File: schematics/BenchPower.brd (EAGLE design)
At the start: 80 x 67 mm, 30 parts, among them U1 V_REG_317SINK, U2 V_REG_317SINK, X2 9090-4R

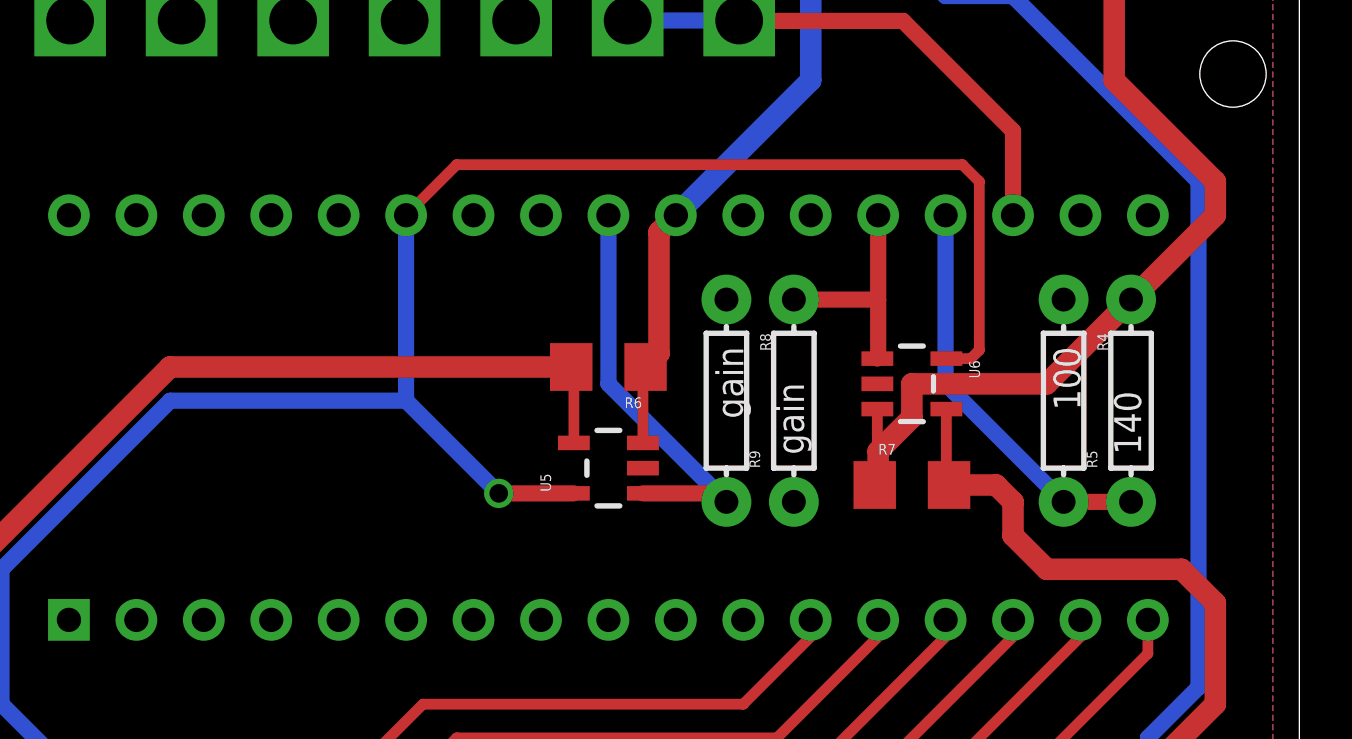
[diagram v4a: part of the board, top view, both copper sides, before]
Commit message: Rework opamp layout
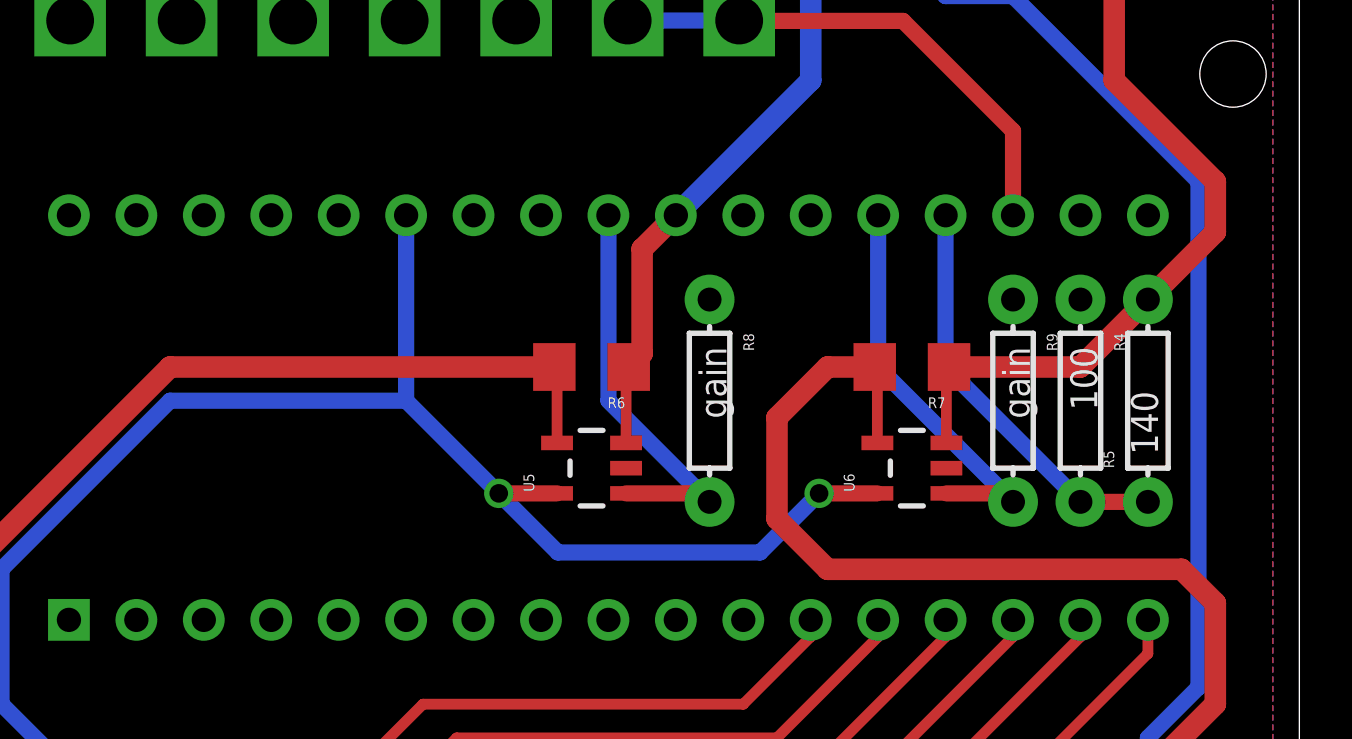
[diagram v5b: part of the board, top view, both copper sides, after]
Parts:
- moved R9 8.26 mm to (69.2, 36.2), turned to 270 degrees
- moved R7 4.45 mm to (65.4, 37.5), turned to 180 degrees
- moved U6 3.17 mm to (65.4, 33.7), turned to 90 degrees
- moved R5 0.64 mm to (74.3, 36.2)
- moved R8 0.64 mm to (57.8, 36.2)
- moved R6 0.63 mm to (53.3, 37.5)
- moved U5 0.63 mm to (53.3, 33.7)
- moved R4 0.63 mm to (71.8, 36.2)
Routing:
- net 5VARDU: track 113.1 -> 98.2 mm, vias 1 -> 2
- net AMPS12VREG: track 48.0 -> 61.5 mm
- net 12VCURRENT: track 8.59 -> 15.5 mm
- net 12VREG: track 49.3 -> 44.8 mm
- net AMPS5VREG: track 56.7 -> 56.1 mm

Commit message: Route signals
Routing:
- net 12VREG: track 44.8 -> 45.5 mm
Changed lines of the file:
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@@
 <wire x1="76.835" y1="44.45" x2="76.835" y2="42.545" width="0.8128" layer="1"/>
 <wire x1="76.835" y1="42.545" x2="74.295" y2="40.005" width="0.8128" layer="1"/>
-<wire x1="74.295" y1="40.005" x2="71.755" y2="37.465" width="0.8128" layer="1"/>
-<wire x1="71.755" y1="37.465" x2="66.805" y2="37.465" width="0.8128" layer="1"/>
+<wire x1="73.025" y1="37.465" x2="66.805" y2="37.465" width="0.8128" layer="1"/>
 <wire x1="66.7051" y1="34.605" x2="66.7051" y2="37.3651" width="0.4064" layer="1"/>
 <wire x1="66.7051" y1="37.3651" x2="66.805" y2="37.465" width="0.4064" layer="1"/>
+<wire x1="73.025" y1="37.465" x2="74.295" y2="38.735" width="0.8128" layer="1"/>
+<wire x1="74.295" y1="38.735" x2="74.295" y2="40.005" width="0.8128" layer="1"/>
 </signal>
 <signal name="ADJREG1">

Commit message: Simplify
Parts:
- removed JP2, JP3: (no value), SparkFun-Connectors:1X03
- removed RV4: (no value), desjardins:POTRK09K111
- removed U2: V_REG_317SINK, SparkFun-PowerIC:TO220-ADJ
- added R10: 140, SparkFun-Passives:AXIAL-0.3
- added S1: EG1213, adafruit:EG1213
- R3: value 240 -> 100
- moved R3 41.2 mm to (50.8, 45.7), turned to 0 degrees
- moved X2 27.4 mm to (12.7, 60.3), turned to 0 degrees
- moved U1 8.48 mm to (77.5, 61.6)
- moved U$1 8.26 mm to (48.3, 55.9)
- moved R2 4.58 mm to (73.0, 55.2), turned to 270 degrees
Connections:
- net 12VCURRENT renamed 12VREGCURRENT
- net 5VCURRENT renamed 12VHDRCURRENT
- net AMPS5VREG renamed AMPS12VHDR
- removed net 12VHDRREG: JP2.3, U1.IN
- removed net 5VHDRREG: JP3.3, U2.IN
- removed net 5VREG: JP3.1, R3.P$2, R6.1, U$2.P25, U2.OUT, U5.3
- removed net ADJREG2: R3.P$1, RV4.P$2, U2.ADJ
- removed net PUSHBUTTON: U$2.P11
- removed net VIN: U$2.P32
- new net 12VHDRSW: R10.P$2, R6.1, S1.2, U1.IN, U5.3
- new net 12VHDRTAP: R10.P$1, R3.P$2, U$2.P25
- net 12VHDR: now also S1.1, U$2.P32; no longer JP2.2
- net 12VREG: no longer JP2.1
- net 5VHDR: no longer JP3.2
- net GND: now also R3.P$1; no longer RV4.P$3
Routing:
- net 12VHDRSW: track 0.00 -> 131.1 mm
- net 5VREG: track 94.2 -> 0.00 mm
- net ADJREG2: track 67.1 -> 0.00 mm
- net 5VHDR: track 138.1 -> 107.5 mm
- net 12VHDR: track 93.3 -> 111.2 mm, vias 0 -> 1
- net 5VHDRREG: track 10.1 -> 0.00 mm
- net 12VHDRREG: track 8.36 -> 0.00 mm
- net 12VREG: track 45.5 -> 39.0 mm
- net 12VHDRTAP: track 0.00 -> 6.35 mm
- net AMPS12VHDR: track 56.1 -> 57.6 mm
- net ADJREG1: track 66.1 -> 64.6 mm
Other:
- board text added: "adj"
- board text removed: "5v"
- board text removed: "bypass"

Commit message: Final pass
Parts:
- removed S1: EG1213, adafruit:EG1213
- added S2: EG1213, desjardins:EG1213
- R1: value 100 -> 1000
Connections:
- net 12VHDR: now also S2.1; no longer S1.1
- net 12VHDRSW: now also R1.P$1, S2.2; no longer S1.2
- net 5VHDR: no longer R1.P$1
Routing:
- net 5VHDR: track 107.5 -> 65.2 mm
- net 12VHDRSW: track 131.1 -> 155.6 mm
- net 12VHDR: track 111.2 -> 108.0 mm
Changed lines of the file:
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@@
 <wire x1="80" y1="67" x2="0" y2="67" width="0" layer="20"/>
 <wire x1="0" y1="67" x2="0" y2="0" width="0" layer="20"/>
-<text x="42.545" y="12.7" size="1.27" layer="21" font="vector">cjd@chrisd.info</text>
-<text x="1.27" y="1.27" size="1.27" layer="21" font="vector">v1.0 (c) 2014</text>
+<text x="43.18" y="12.7" size="1.524" layer="21">cjd@chrisd.info</text>
+<text x="1.27" y="1.27" size="1.27" layer="21">v1.0 (c) 2014</text>
 <wire x1="13.97" y1="5.715" x2="13.97" y2="5.97" width="0.4064" layer="21"/>
 <wire x1="13.97" y1="5.97" x2="20" y2="12" width="0.4064" layer="21" curve="-90"/>
@@
 <wire x1="60" y1="0" x2="47" y2="0" width="0.4064" layer="21"/>
 <wire x1="47" y1="0" x2="41" y2="6" width="0.4064" layer="21" curve="-90"/>
-<text x="52.07" y="1.27" size="1.27" layer="21" font="vector">adj</text>
-<text x="24.765" y="1.27" size="1.27" layer="21" font="vector">12v</text>
-<text x="10.795" y="12.7" size="1.27" layer="21" font="vector">blog.chrisd.info</text>
+<text x="52.07" y="1.27" size="1.27" layer="21">adj</text>
+<text x="24.765" y="1.27" size="1.27" layer="21">12v</text>
+<text x="10.795" y="12.7" size="1.524" layer="21">blog.chrisd.info</text>
 </plain>
 <attributes>
@@
 <element name="U$2" library="ChrisD" package="ARDUINO_PRO_MICRO" value="ARDUINO_PRO_MICRO" x="78.105" y="26.67" rot="R90"/>
 <element name="U1" library="SparkFun-PowerIC" package="TO220-ADJ" value="V_REG_317SINK" x="77.47" y="61.595" rot="R90"/>
-<element name="R1" library="SparkFun-Passives" package="AXIAL-0.3" value="100" x="32.385" y="13.335"/>
+<element name="R1" library="SparkFun-Passives" package="AXIAL-0.3" value="1000" x="32.385" y="13.335"/>
 <element name="R2" library="SparkFun-Passives" package="AXIAL-0.3" value="240" x="73.025" y="55.245" rot="R270"/>
 <element name="U$3" library="desjardins" package="LOGO" value="" x="58.42" y="12.7"/>
@@
 <element name="R3" library="SparkFun-Passives" package="AXIAL-0.3" value="100" x="50.8" y="45.72"/>
 <element name="R10" library="SparkFun-Passives" package="AXIAL-0.3" value="140" x="62.23" y="45.72"/>
-<element name="S1" library="adafruit" package="EG1213" value="EG1213" x="2.54" y="27.305" rot="R270"/>
+<element name="S2" library="desjardins" package="EG1213" value="EG1213" x="6.35" y="26.035" rot="R270"/>
 </elements>
 <signals>
@@
 <contactref element="X2" pad="4"/>
 <contactref element="U$2" pad="P20"/>
-<contactref element="R1" pad="P$1"/>
 <wire x1="20.32" y1="53.975" x2="21.59" y2="52.705" width="0.6096" layer="16"/>
 <wire x1="21.59" y1="52.705" x2="41.91" y2="52.705" width="0.6096" layer="16"/>
@@
 <wire x1="67.16" y1="50.315" x2="69.215" y2="48.26" width="0.6096" layer="16"/>
 <wire x1="69.215" y1="48.26" x2="69.215" y2="43.18" width="0.6096" layer="16"/>
-<wire x1="21.59" y1="52.705" x2="21.59" y2="20.32" width="0.6096" layer="16"/>
-<wire x1="21.59" y1="20.32" x2="28.575" y2="13.335" width="0.6096" layer="16"/>
 </signal>
 <signal name="3V3">
@@
 <contactref element="U$2" pad="P32"/>
 <wire x1="5.08" y1="53.975" x2="5.08" y2="52.07" width="0.8128" layer="1"/>
-<contactref element="S1" pad="1"/>
 <wire x1="5.08" y1="52.07" x2="6.35" y2="50.8" width="0.8128" layer="1"/>
 <wire x1="6.35" y1="50.8" x2="6.35" y2="48.895" width="0.8128" layer="1"/>
-<wire x1="6.35" y1="48.895" x2="6.35" y2="30.48" width="0.8128" layer="1"/>
-<wire x1="6.35" y1="30.48" x2="5.08" y2="29.21" width="0.8128" layer="1"/>
-<wire x1="5.08" y1="29.21" x2="2.635" y2="29.21" width="0.8128" layer="1"/>
-<wire x1="2.635" y1="29.21" x2="2.54" y2="29.305" width="0.8128" layer="1"/>
 <wire x1="67.16" y1="55.88" x2="67.16" y2="54.46" width="0.8128" layer="1"/>
 <wire x1="67.16" y1="54.46" x2="66.04" y2="53.34" width="0.8128" layer="1"/>
@@
 <wire x1="25.4" y1="48.895" x2="6.35" y2="48.895" width="0.8128" layer="1"/>
 <via x="27.305" y="46.99" extent="1-16" drill="0.7"/>
+<contactref element="S2" pad="1"/>
+<wire x1="6.35" y1="48.895" x2="6.35" y2="29.305" width="0.8128" layer="1"/>
 </signal>
 <signal name="N$1">
 <contactref element="R1" pad="P$2"/>
 <contactref element="LED1" pad="A"/>
-<wire x1="36.195" y1="13.335" x2="36.195" y2="12.7" width="0.6096" layer="16"/>
-<wire x1="36.195" y1="12.7" x2="36.83" y2="12.065" width="0.6096" layer="16"/>
-<wire x1="36.83" y1="12.065" x2="38.735" y2="12.065" width="0.6096" layer="16"/>
+<wire x1="36.195" y1="13.335" x2="36.195" y2="12.7" width="0.4064" layer="16"/>
+<wire x1="36.195" y1="12.7" x2="36.83" y2="12.065" width="0.4064" layer="16"/>
+<wire x1="36.83" y1="12.065" x2="38.735" y2="12.065" width="0.4064" layer="16"/>
 </signal>
 <signal name="PWR_OK">
@@
 <wire x1="54.6401" y1="37.3651" x2="54.74" y2="37.465" width="0.6096" layer="1"/>
 <contactref element="R10" pad="P$2"/>
-<contactref element="S1" pad="2"/>
-<wire x1="2.54" y1="27.305" x2="17.78" y2="27.305" width="0.8128" layer="1"/>
-<wire x1="17.78" y1="27.305" x2="31.115" y2="40.64" width="0.8128" layer="1"/>
+<wire x1="16.51" y1="26.035" x2="31.115" y2="40.64" width="0.8128" layer="1"/>
 <wire x1="31.115" y1="40.64" x2="53.975" y2="40.64" width="0.8128" layer="1"/>
 <wire x1="53.975" y1="40.64" x2="55.245" y2="39.37" width="0.8128" layer="1"/>
@@
 <wire x1="66.04" y1="45.72" x2="66.04" y2="47.625" width="0.8128" layer="1"/>
 <wire x1="54.6401" y1="34.605" x2="54.6401" y2="37.3651" width="0.4064" layer="1"/>
+<contactref element="S2" pad="2"/>
+<wire x1="16.51" y1="26.035" x2="6.35" y2="26.035" width="0.8128" layer="1"/>
+<contactref element="R1" pad="P$1"/>
+<wire x1="28.575" y1="13.335" x2="28.575" y2="13.97" width="0.4064" layer="16"/>
+<wire x1="28.575" y1="13.97" x2="16.51" y2="26.035" width="0.4064" layer="16"/>
+<wire x1="16.51" y1="26.035" x2="6.35" y2="26.035" width="0.4064" layer="16"/>
 </signal>
 </signals>
